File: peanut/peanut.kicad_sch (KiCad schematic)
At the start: 39 parts, among them J1 USB-C, Q1 NMOS, U1 MS5611-01BA, U3 ESP32-C3FH4, Y1 40MHz +/-10ppm

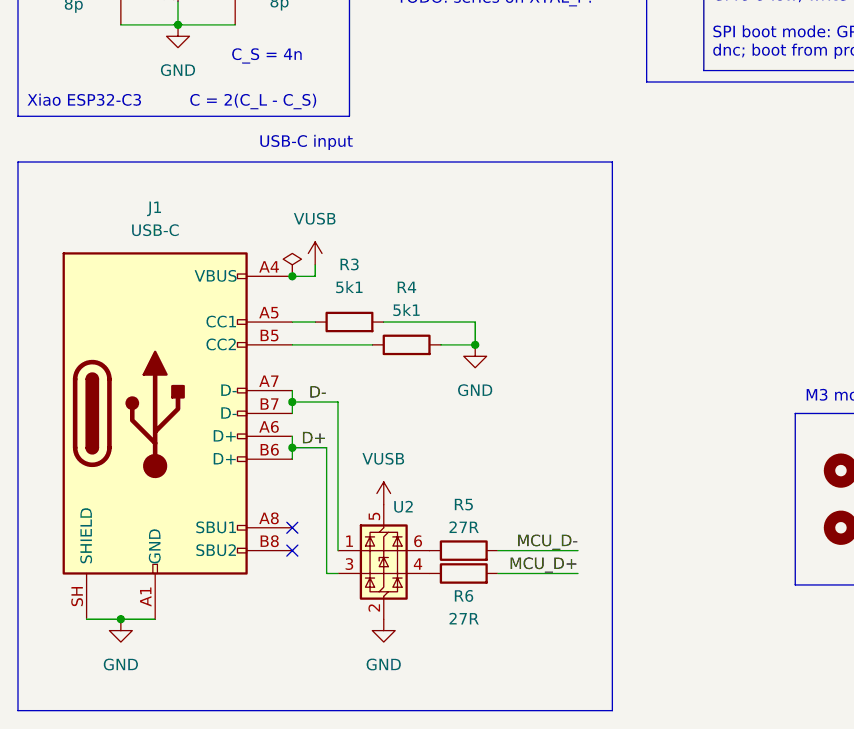
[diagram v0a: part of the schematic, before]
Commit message: feat: Initial routing
Initial, rough routing of traces.
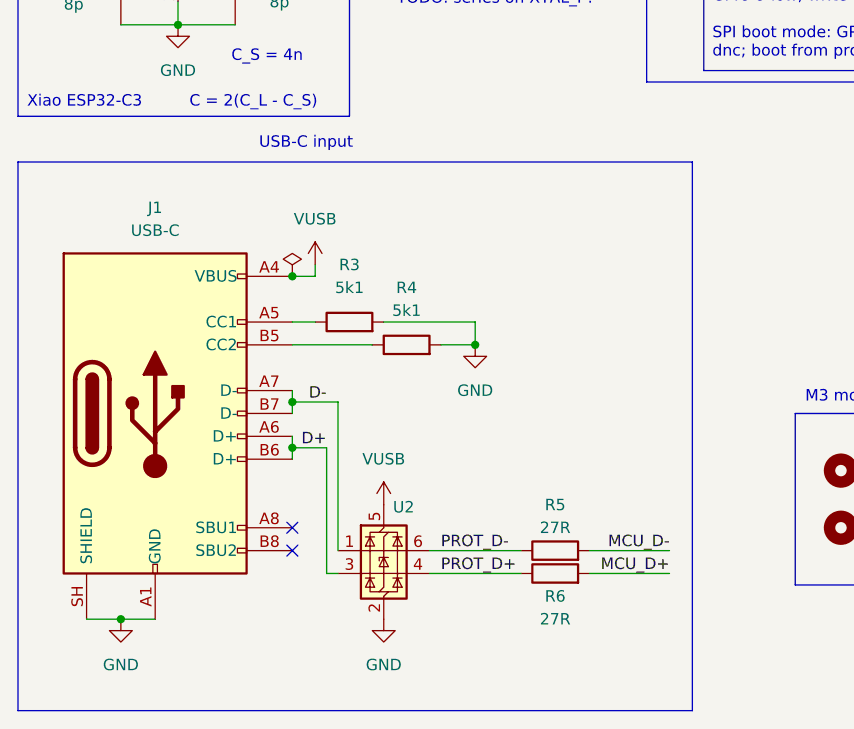
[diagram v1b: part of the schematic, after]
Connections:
- net PROT_D+: now reaches R6.1, U2.4 (I/O2)
- net PROT_D-: now reaches R5.1, U2.6 (I/O1)
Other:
- moved on the sheet: R5, R6
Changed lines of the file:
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@@
 	(rectangle
 		(start 15.24 134.62)
-		(end 81.28 195.58)
+		(end 90.17 195.58)
 		(stroke
 			(width 0)
@@
 	(wire
 		(pts
+			(xy 60.96 177.8) (xy 71.12 177.8)
+		)
+		(stroke
+			(width 0)
+			(type default)
+		)
+	)
+	(wire
+		(pts
 			(xy 147.32 53.34) (xy 147.32 60.96)
 		)
@@
 	(wire
 		(pts
-			(xy 68.58 177.8) (xy 77.47 177.8)
+			(xy 78.74 177.8) (xy 87.63 177.8)
 		)
 		(stroke
@@
 	(wire
 		(pts
-			(xy 68.58 180.34) (xy 77.47 180.34)
+			(xy 78.74 180.34) (xy 87.63 180.34)
 		)
 		(stroke
@@
 	(wire
 		(pts
+			(xy 71.12 180.34) (xy 60.96 180.34)
+		)
+		(stroke
+			(width 0)
+			(type default)
+		)
+	)
+	(wire
+		(pts
 			(xy 124.46 88.9) (xy 114.3 88.9)
 		)
@@
 	)
 	(label "MCU_D+"
-		(at 77.47 180.34 180)
+		(at 87.63 180.34 180)
 		(effects
 			(font
@@
 		)
 	)
+	(label "PROT_D-"
+		(at 62.23 177.8 0)
+		(effects
+			(font
+				(size 1.27 1.27)
+			)
+			(justify left bottom)
+		)
+	)
 	(label "I2C_SDA"
 		(at 19.05 38.1 0)
@@
 		)
 	)
+	(label "PROT_D+"
+		(at 62.23 180.34 0)
+		(effects
+			(font
+				(size 1.27 1.27)
+			)
+			(justify left bottom)
+		)
+	)
 	(label "I2C_SDA"
 		(at 179.07 81.28 180)
@@
 	)
 	(label "MCU_D-"
-		(at 77.47 177.8 180)
+		(at 87.63 177.8 180)
 		(effects
 			(font
@@
 	(symbol
 		(lib_id "Device:R")
-		(at 64.77 180.34 90)
+		(at 74.93 180.34 90)
 		(unit 1)
 		(body_style 1)
@@
 		(dnp no)
 		(property "Reference" "R6"
-			(at 64.77 182.88 90)
+			(at 74.93 182.88 90)
 			(show_name no)
 			(do_not_autoplace no)
@@
 		)
 		(property "Value" "27R"
-			(at 64.77 185.42 90)
+			(at 74.93 185.42 90)
 			(show_name no)
 			(do_not_autoplace no)
@@
 		)
 		(property "Footprint" "Resistor_SMD:R_0402_1005Metric"
-			(at 64.77 182.118 90)
+			(at 74.93 182.118 90)
 			(hide yes)
 			(show_name no)
@@
 		)
 		(property "Datasheet" ""
-			(at 64.77 180.34 0)
+			(at 74.93 180.34 0)
 			(hide yes)
 			(show_name no)
@@
 		)
 		(property "Description" "Resistor"
-			(at 64.77 180.34 0)
+			(at 74.93 180.34 0)
 			(hide yes)
 			(show_name no)
@@
 		)
 		(property "MPN" "ERA-2AKD270X"
-			(at 64.77 180.34 90)
+			(at 74.93 180.34 90)
 			(hide yes)
 			(show_name no)
@@
 	(symbol
 		(lib_id "Device:R")
-		(at 64.77 177.8 90)
+		(at 74.93 177.8 90)
 		(unit 1)
 		(body_style 1)
@@
 		(dnp no)
 		(property "Reference" "R5"
-			(at 64.77 172.72 90)
+			(at 74.93 172.72 90)
 			(show_name no)
 			(do_not_autoplace no)
@@
 		)
 		(property "Value" "27R"
-			(at 64.77 175.26 90)
+			(at 74.93 175.26 90)
 			(show_name no)
 			(do_not_autoplace no)
@@
 		)
 		(property "Footprint" "Resistor_SMD:R_0402_1005Metric"
-			(at 64.77 179.578 90)
+			(at 74.93 179.578 90)
 			(hide yes)
 			(show_name no)
@@
 		)
 		(property "Datasheet" ""
-			(at 64.77 177.8 0)
+			(at 74.93 177.8 0)
 			(hide yes)
 			(show_name no)
@@
 		)
 		(property "Description" "Resistor"
-			(at 64.77 177.8 0)
+			(at 74.93 177.8 0)
 			(hide yes)
 			(show_name no)
@@
 		)
 		(property "MPN" "ERA-2AKD270X"
-			(at 64.77 177.8 90)
+			(at 74.93 177.8 90)
 			(hide yes)
 			(show_name no)

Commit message: feat: Route the Bluetooth trace
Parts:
- C12, C13: footprint Capacitor_SMD:C_0201_0603Metric_Pad0.64x0.40mm_HandSolder -> Capacitor_SMD:C_0201_0603Metric
- L2: footprint Inductor_SMD:L_0201_0603Metric_Pad0.64x0.40mm_HandSolder -> Inductor_SMD:L_0201_0603Metric
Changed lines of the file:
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@@
 			)
 		)
-		(property "Footprint" "Inductor_SMD:L_0201_0603Metric_Pad0.64x0.40mm_HandSolder"
+		(property "Footprint" "Inductor_SMD:L_0201_0603Metric"
 			(at 237.49 38.1 0)
 			(hide yes)
@@
 			)
 		)
-		(property "Footprint" "Capacitor_SMD:C_0201_0603Metric_Pad0.64x0.40mm_HandSolder"
+		(property "Footprint" "Capacitor_SMD:C_0201_0603Metric"
 			(at 232.1052 45.72 0)
 			(hide yes)
@@
 			)
 		)
-		(property "Footprint" "Capacitor_SMD:C_0201_0603Metric_Pad0.64x0.40mm_HandSolder"
+		(property "Footprint" "Capacitor_SMD:C_0201_0603Metric"
 			(at 244.8052 45.72 0)
 			(hide yes)

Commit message: chore: fix inductor footprint size
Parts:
- L1: footprint Inductor_SMD:L_01005_0402Metric -> Inductor_SMD:L_0402_1005Metric
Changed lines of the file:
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@@
 			)
 		)
-		(property "Footprint" "Inductor_SMD:L_01005_0402Metric"
+		(property "Footprint" "Inductor_SMD:L_0402_1005Metric"
 			(at 114.3 33.02 0)
 			(hide yes)

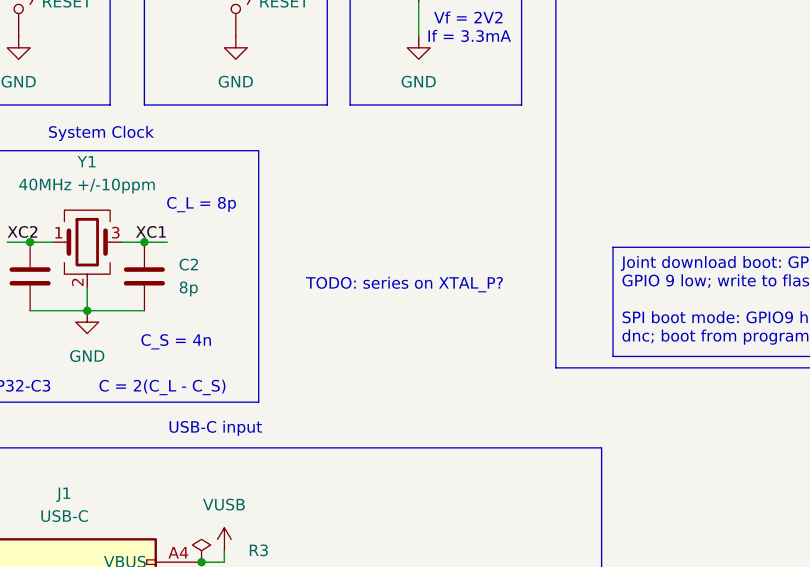
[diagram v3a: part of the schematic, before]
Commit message: feat: Move USB closer to the edge.
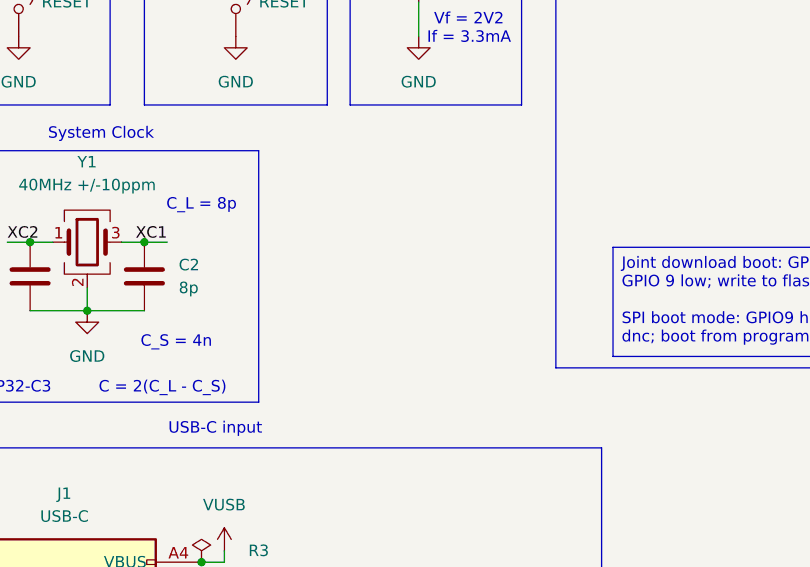
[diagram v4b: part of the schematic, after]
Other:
- note removed: "TODO: series on XTAL_P?"
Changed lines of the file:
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@@
-		)
-	)
-	(text "TODO: series on XTAL_P?"
-		(exclude_from_sim no)
-		(at 68.326 116.586 0)
-		(effects
-			(font
-				(size 1.27 1.27)
-			)
 		)
 	)

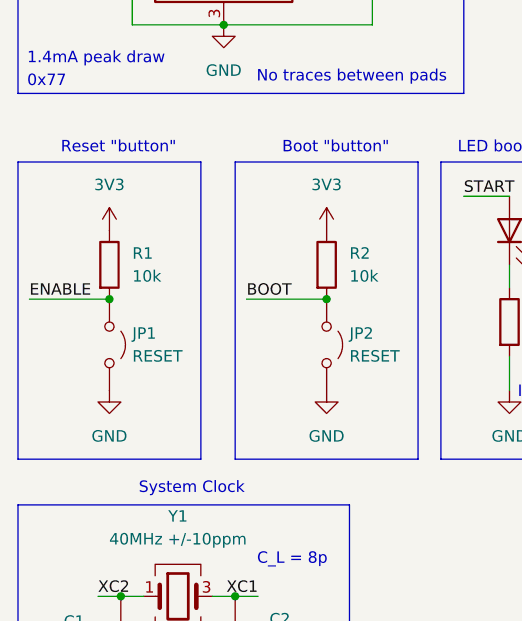
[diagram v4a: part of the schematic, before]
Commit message: chore: add CHIP_EN capacitor
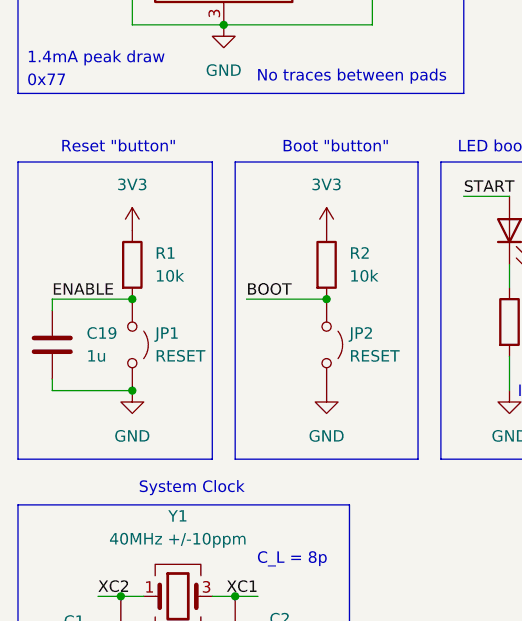
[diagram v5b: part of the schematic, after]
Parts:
- added C19: 1u, Capacitor_SMD:C_0603_1608Metric, symbol Device:C
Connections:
- net ENABLE: now also C19.1
- net GND: now also C19.2
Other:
- moved on the sheet: JP1, R1
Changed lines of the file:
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@@
 	(rectangle
 		(start 15.24 63.5)
-		(end 35.56 96.52)
+		(end 36.83 96.52)
 		(stroke
 			(width 0)
@@
 	)
 	(junction
+		(at 27.94 88.9)
+		(diameter 0)
+		(color 0 0 0 0)
+	)
+	(junction
 		(at 49.53 78.74)
 		(diameter 0)
@@
 	)
 	(junction
-		(at 25.4 78.74)
+		(at 27.94 78.74)
 		(diameter 0)
 		(color 0 0 0 0)
@@
 	(wire
 		(pts
+			(xy 19.05 88.9) (xy 19.05 87.63)
+		)
+		(stroke
+			(width 0)
+			(type default)
+		)
+	)
+	(wire
+		(pts
 			(xy 22.86 185.42) (xy 26.67 185.42)
 		)
@@
 	(wire
 		(pts
+			(xy 19.05 80.01) (xy 19.05 78.74)
+		)
+		(stroke
+			(width 0)
+			(type default)
+		)
+	)
+	(wire
+		(pts
 			(xy 120.65 33.02) (xy 125.73 33.02)
 		)
@@
 	(wire
 		(pts
+			(xy 19.05 88.9) (xy 27.94 88.9)
+		)
+		(stroke
+			(width 0)
+			(type default)
+		)
+	)
+	(wire
+		(pts
 			(xy 157.48 58.42) (xy 157.48 60.96)
 		)
@@
 	(wire
 		(pts
-			(xy 16.51 78.74) (xy 25.4 78.74)
+			(xy 19.05 78.74) (xy 27.94 78.74)
 		)
 		(stroke
@@
 	)
 	(label "ENABLE"
-		(at 16.51 78.74 0)
+		(at 19.05 78.74 0)
 		(effects
 			(font
@@
 	(symbol
 		(lib_id "power:GND")
-		(at 25.4 88.9 0)
+		(at 27.94 88.9 0)
 		(unit 1)
 		(body_style 1)
@@
 		(fields_autoplaced yes)
 		(property "Reference" "#PWR02"
-			(at 25.4 95.25 0)
+			(at 27.94 95.25 0)
 			(hide yes)
 			(show_name no)
@@
 		)
 		(property "Value" "GND"
-			(at 25.4 93.98 0)
+			(at 27.94 93.98 0)
 			(show_name no)
 			(do_not_autoplace no)
@@
 		)
 		(property "Footprint" ""
-			(at 25.4 88.9 0)
+			(at 27.94 88.9 0)
 			(hide yes)
 			(show_name no)
@@
 		)
 		(property "Datasheet" ""
-			(at 25.4 88.9 0)
+			(at 27.94 88.9 0)
 			(hide yes)
 			(show_name no)
@@
 		)
 		(property "Description" "Power symbol creates a global label with name \"GND\" , ground"
-			(at 25.4 88.9 0)
+			(at 27.94 88.9 0)
 			(hide yes)
 			(show_name no)
@@
 	(symbol
 		(lib_id "Device:R")
-		(at 25.4 74.93 0)
+		(at 27.94 74.93 0)
 		(unit 1)
 		(body_style 1)
@@
 		(fields_autoplaced yes)
 		(property "Reference" "R1"
-			(at 27.94 73.6599 0)
+			(at 30.48 73.6599 0)
 			(show_name no)
 			(do_not_autoplace no)
@@
 		)
 		(property "Value" "10k"
-			(at 27.94 76.1999 0)
+			(at 30.48 76.1999 0)
 			(show_name no)
 			(do_not_autoplace no)
@@
 		)
 		(property "Footprint" "Resistor_SMD:R_0402_1005Metric"
-			(at 23.622 74.93 90)
+			(at 26.162 74.93 90)
 			(hide yes)
 			(show_name no)
@@
 		)
 		(property "Datasheet" ""
-			(at 25.4 74.93 0)
+			(at 27.94 74.93 0)
 			(hide yes)
 			(show_name no)
@@
 		)
 		(property "Description" "Resistor"
-			(at 25.4 74.93 0)
+			(at 27.94 74.93 0)
 			(hide yes)
 			(show_name no)
@@
 		)
 		(property "MPN" "MCS04020C1002FE000"
-			(at 25.4 74.93 0)
+			(at 27.94 74.93 0)
 			(hide yes)
 			(show_name no)
@@
 	(symbol
 		(lib_id "Jumper:Jumper_2_Open")
-		(at 25.4 83.82 270)
+		(at 27.94 83.82 270)
 		(unit 1)
 		(body_style 1)
@@
 		(fields_autoplaced yes)
 		(property "Reference" "JP1"
-			(at 27.94 82.5499 90)
+			(at 30.48 82.5499 90)
 			(show_name no)
 			(do_not_autoplace no)
@@
 		)
 		(property "Value" "RESET"
-			(at 27.94 85.0899 90)
+			(at 30.48 85.0899 90)
 			(show_name no)
 			(do_not_autoplace no)
@@
 		)
 		(property "Footprint" "Jumper:SolderJumper-2_P1.3mm_Open_TrianglePad1.0x1.5mm"
-			(at 25.4 83.82 0)
+			(at 27.94 83.82 0)
 			(hide yes)
 			(show_name no)
@@
 		)
 		(property "Datasheet" ""
-			(at 25.4 83.82 0)
+			(at 27.94 83.82 0)
 			(hide yes)
 			(show_name no)
@@
 		)
 		(property "Description" "Jumper, 2-pole, open"
-			(at 25.4 83.82 0)
+			(at 27.94 83.82 0)
 			(hide yes)
 			(show_name no)
@@
 		)
 		(property "MPN" ""
-			(at 25.4 83.82 90)
+			(at 27.94 83.82 90)
 			(hide yes)
 			(show_name no)
@@
 	)
 	(symbol
+		(lib_id "Device:C")
+		(at 19.05 83.82 0)
+		(unit 1)
+		(body_style 1)
+		(exclude_from_sim no)
+		(in_bom yes)
+		(on_board yes)
+		(in_pos_files yes)
+		(dnp no)
+		(fields_autoplaced yes)
+		(property "Reference" "C19"
+			(at 22.86 82.5499 0)
+			(show_name no)
+			(do_not_autoplace no)
+			(effects
+				(font
+					(size 1.27 1.27)
+				)
+				(justify left)
+			)
+		)
+		(property "Value" "1u"
+			(at 22.86 85.0899 0)
+			(show_name no)
+			(do_not_autoplace no)
+			(effects
+				(font
+					(size 1.27 1.27)
+				)
+				(justify left)
+			)
+		)
+		(property "Footprint" "Capacitor_SMD:C_0603_1608Metric"
+			(at 20.0152 87.63 0)
+			(hide yes)
+			(show_name no)
+			(do_not_autoplace no)
+			(effects
+				(font
+					(size 1.27 1.27)
+				)
+			)
+		)
+		(property "Datasheet" ""
+			(at 19.05 83.82 0)
+			(hide yes)
+			(show_name no)
+			(do_not_autoplace no)
+			(effects
+				(font
+					(size 1.27 1.27)
+				)
+			)
+		)
+		(property "Description" "Unpolarized capacitor"
+			(at 19.05 83.82 0)
+			(hide yes)
+			(show_name no)
+			(do_not_autoplace no)
+			(effects
+				(font
+					(size 1.27 1.27)
+				)
+			)
+		)
+		(property "MPN" "06036C105MAT2A"
+			(at 19.05 83.82 0)
+			(hide yes)
+			(show_name no)
+			(do_not_autoplace no)
+			(effects
+				(font
+					(size 1.27 1.27)
+				)
+			)
+		)
+		(pin "2"
+		)
+		(pin "1"
+		)
+		(instances
+			(project "peanut"
+				(path "/5c6b6cfc-6c84-425a-9b66-e6111713aae8"
+					(reference "C19")
+					(unit 1)
+				)
+			)
+		)
+	)
+	(symbol
 		(lib_id "power:VBUS")
-		(at 25.4 71.12 0)
+		(at 27.94 71.12 0)
 		(unit 1)
 		(body_style 1)
@@
 		(fields_autoplaced yes)
 		(property "Reference" "#PWR01"
-			(at 25.4 74.93 0)
+			(at 27.94 74.93 0)
 			(hide yes)
 			(show_name no)
@@
 		)
 		(property "Value" "3V3"
-			(at 25.4 66.04 0)
+			(at 27.94 66.04 0)
 			(show_name no)
 			(do_not_autoplace no)
@@
 		)
 		(property "Footprint" ""
-			(at 25.4 71.12 0)
+			(at 27.94 71.12 0)
 			(hide yes)
 			(show_name no)
@@
 		)
 		(property "Datasheet" ""
-			(at 25.4 71.12 0)
+			(at 27.94 71.12 0)
 			(hide yes)
 			(show_name no)
@@
 		)
 		(property "Description" "Power symbol creates a global label with name \"VBUS\""
-			(at 25.4 71.12 0)
+			(at 27.94 71.12 0)
 			(hide yes)
 			(show_name no)

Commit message: chore: add flyback diode to buzzer
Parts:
- added D5: (no value), Diode_SMD:D_SOD-123F, symbol Device:D_Schottky
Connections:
- net 3V3: now also D5.1 (K)
- net at BZ1.2 (-), Q1.3 (D): now also D5.2 (A)
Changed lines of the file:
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@@
 	(text "Max: 30mA"
 		(exclude_from_sim no)
-		(at 225.298 76.2 0)
+		(at 241.554 66.548 0)
 		(effects
 			(font
@@
 	)
 	(junction
+		(at 232.41 72.39)
+		(diameter 0)
+		(color 0 0 0 0)
+	)
+	(junction
+		(at 232.41 80.01)
+		(diameter 0)
+		(color 0 0 0 0)
+	)
+	(junction
 		(at 45.72 147.32)
 		(diameter 0)
@@
 	(wire
 		(pts
+			(xy 226.06 80.01) (xy 232.41 80.01)
+		)
+		(stroke
+			(width 0)
+			(type default)
+		)
+	)
+	(wire
+		(pts
 			(xy 54.61 30.48) (xy 54.61 27.94)
 		)
@@
 	(wire
 		(pts
+			(xy 232.41 72.39) (xy 232.41 73.66)
+		)
+		(stroke
+			(width 0)
+			(type default)
+		)
+	)
+	(wire
+		(pts
 			(xy 123.19 63.5) (xy 124.46 63.5)
 		)
@@
 	(wire
 		(pts
+			(xy 226.06 72.39) (xy 232.41 72.39)
+		)
+		(stroke
+			(width 0)
+			(type default)
+		)
+	)
+	(wire
+		(pts
 			(xy 39.37 111.76) (xy 36.83 111.76)
 		)
@@
 	(wire
 		(pts
-			(xy 232.41 69.85) (xy 232.41 73.66)
-		)
-		(stroke
-			(width 0)
-			(type default)
-		)
-	)
-	(wire
-		(pts
 			(xy 27.94 33.02) (xy 27.94 27.94)
 		)
@@
 		(pts
 			(xy 71.12 180.34) (xy 60.96 180.34)
+		)
+		(stroke
+			(width 0)
+			(type default)
+		)
+	)
+	(wire
+		(pts
+			(xy 232.41 69.85) (xy 232.41 72.39)
 		)
 		(stroke
@@
 					(unit 1)
 				)
+			)
+		)
+	)
+	(symbol
+		(lib_id "Device:D_Schottky")
+		(at 226.06 76.2 270)
+		(unit 1)
+		(body_style 1)
+		(exclude_from_sim no)
+		(in_bom yes)
+		(on_board yes)
+		(in_pos_files yes)
+		(dnp no)
+		(fields_autoplaced yes)
+		(property "Reference" "D5"
+			(at 228.6 75.8824 90)
+			(show_name no)
+			(do_not_autoplace no)
+			(effects
+				(font
+					(size 1.27 1.27)
+				)
+				(justify left)
+			)
+		)
+		(property "Value" ""
+			(at 228.6 77.1524 90)
+			(show_name no)
+			(do_not_autoplace no)
+			(effects
+				(font
+					(size 1.27 1.27)
+				)
+				(justify left)
+			)
+		)
+		(property "Footprint" "Diode_SMD:D_SOD-123F"
+			(at 226.06 76.2 0)
+			(hide yes)
+			(show_name no)
+			(do_not_autoplace no)
+			(effects
+				(font
+					(size 1.27 1.27)
+				)
+			)
+		)
+		(property "Datasheet" "https://www.onsemi.com/pub/Collateral/SS29FA-D.PDF"
+			(at 226.06 76.2 0)
+			(hide yes)
+			(show_name no)
+			(do_not_autoplace no)
+			(effects
+				(font
+					(size 1.27 1.27)
+				)
+			)
+		)
+		(property "Description" "Schottky diode"
+			(at 226.06 76.2 0)
+			(hide yes)
+			(show_name no)
+			(do_not_autoplace no)
+			(effects
+				(font
+					(size 1.27 1.27)
+				)
+			)
+		)
+		(property "MPN" "SS25FA"
+			(at 226.06 76.2 90)
+			(hide yes)
+			(show_name no)
+			(do_not_autoplace no)
+			(effects
+				(font
+					(size 1.27 1.27)
+				)
+			)
+		)
+		(pin "2"
+		)
+		(pin "1"
+		)
+		(instances
+			(project "peanut"
+				(path "/5c6b6cfc-6c84-425a-9b66-e6111713aae8"
+					(reference "D5")
+					(unit 1)
+				)

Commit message: chore: updated RF components to 0402
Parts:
- C12, C13: footprint Capacitor_SMD:C_0201_0603Metric -> Capacitor_SMD:C_0402_1005Metric; MPN GRM0335C1H1R6BA01D -> RF15N1R6B500CT
- L2: footprint Inductor_SMD:L_0201_0603Metric -> Capacitor_SMD:C_0402_1005Metric; MPN LQP03TN2N6B02D -> LQG15WZ2N6B02D
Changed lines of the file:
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@@
 			)
 		)
-		(property "Footprint" "Inductor_SMD:L_0201_0603Metric"
+		(property "Footprint" "Capacitor_SMD:C_0402_1005Metric"
 			(at 237.49 38.1 0)
 			(hide yes)
@@
 			)
 		)
-		(property "Datasheet" "https://www.mouser.ca/datasheet/3/76/2/JELF243C_0015.pdf"
+		(property "Datasheet" "https://www.mouser.ca/datasheet/3/76/2/JELF243B_9117.pdf"
 			(at 237.49 38.1 0)
 			(hide yes)
@@
 			)
 		)
-		(property "MPN" "LQP03TN2N6B02D"
+		(property "MPN" "LQG15WZ2N6B02D"
 			(at 237.49 38.1 90)
 			(hide yes)
@@
 			)
 		)
-		(property "Footprint" "Capacitor_SMD:C_0201_0603Metric"
+		(property "Footprint" "Capacitor_SMD:C_0402_1005Metric"
 			(at 232.1052 45.72 0)
 			(hide yes)
@@
 			)
 		)
-		(property "Datasheet" "https://www.mouser.ca/datasheet/3/76/2/GRM0335C1H1R6BA01_01A.pdf"
+		(property "Datasheet" "https://www.mouser.ca/datasheet/3/317/1/Microwave_Caps.pdf"
 			(at 231.14 41.91 0)
 			(hide yes)
@@
 			)
 		)
-		(property "MPN" "GRM0335C1H1R6BA01D"
+		(property "MPN" "RF15N1R6B500CT"
 			(at 231.14 41.91 0)
 			(hide yes)
@@
 			)
 		)
-		(property "Footprint" "Capacitor_SMD:C_0201_0603Metric"
+		(property "Footprint" "Capacitor_SMD:C_0402_1005Metric"
 			(at 244.8052 45.72 0)
 			(hide yes)
@@
 			)
 		)
-		(property "Datasheet" "https://www.mouser.ca/datasheet/3/76/2/GRM0335C1H1R6BA01_01A.pdf"
+		(property "Datasheet" "https://www.mouser.ca/datasheet/3/317/1/Microwave_Caps.pdf"
 			(at 243.84 41.91 0)
 			(hide yes)
@@
 			)
 		)
-		(property "MPN" "GRM0335C1H1R6BA01D"
+		(property "MPN" "RF15N1R6B500CT"
 			(at 243.84 41.91 0)
 			(hide yes)
